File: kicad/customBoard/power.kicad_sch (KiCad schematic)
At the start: 30 parts

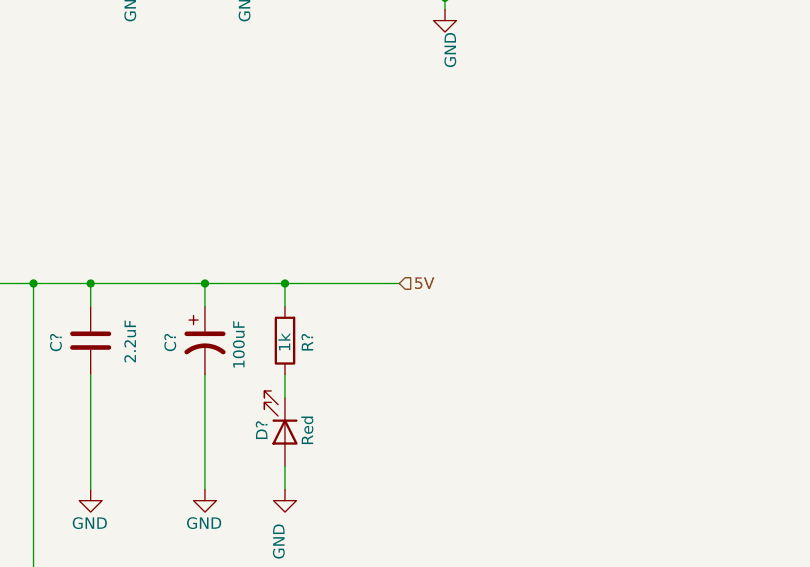
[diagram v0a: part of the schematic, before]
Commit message: First draft of CM4_GPIO
The CM4 connectors are split into two units. This is the right unit, name GPIO. Next is the left, High Speed Serial unit.
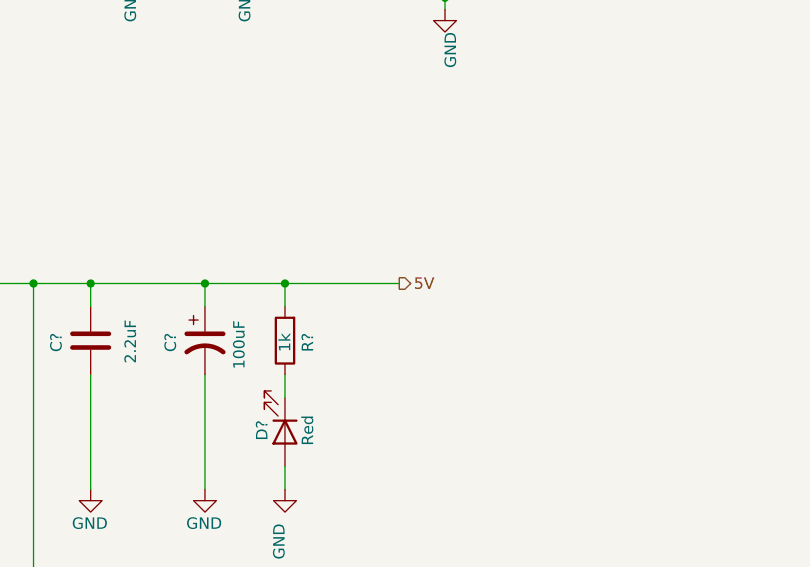
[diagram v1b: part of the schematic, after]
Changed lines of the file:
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@@
     (stroke (width 0) (type solid) (color 0 0 0 0))
   )
-  (hierarchical_label "5V" (shape input) (at 177.8 101.6 0)
+  (hierarchical_label "5V" (shape output) (at 177.8 101.6 0)
     (effects (font (size 1.27 1.27)) (justify left))
   )

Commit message: Generate Netlist
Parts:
- B1: renamed from B?; footprint (none) -> JSTPH2:JSTPH2
- C1, C2, C3, C4, C5, C6: renamed from C?; footprint (none) -> Capacitor_SMD:C_1206_3216Metric_Pad1.33x1.80mm_HandSolder
- D1, D2, D3, D4: renamed from D?; footprint (none) -> digikey-footprints:LED_5mm_Radial
- J1: renamed from J?; footprint GCT_USB4125-GF-A_REVA2 -> USB4125-GF-A_REVA2:GCT_USB4125-GF-A_REVA2
- L1: renamed from L?; footprint (none) -> NRS5030T6R8MMGJ:NRS5030T6R8MMGJ
- Q1: renamed from Q?; footprint SOT95P240X111-3N -> MMUN2133LT1G:SOT95P240X111-3N
- R1, R10, R11, R12, R13, R14, R2, R3, R4, R5, R6, R7, R8, R9: renamed from R?; footprint (none) -> Resistor_SMD:R_1206_3216Metric_Pad1.30x1.75mm_HandSolder
- U1: renamed from U?; footprint QFN65P400X400X100-17N -> TPS61090RSAR:QFN65P400X400X100-17N
- gave numbers to parts that had none: 1
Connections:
- no-connect marks 0 -> 1

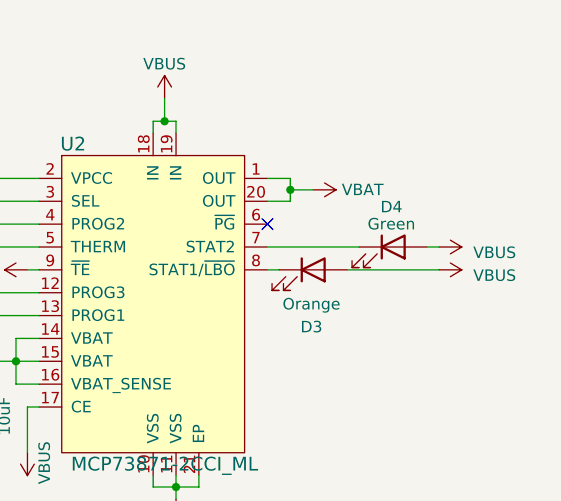
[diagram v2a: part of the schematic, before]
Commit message: Rework Power PCB and draft SD
Moving things around so they would make sense on the final board. Flipped around some of the power circuit so the battery can be plugged in on the left side to make room for all the ports on the right.
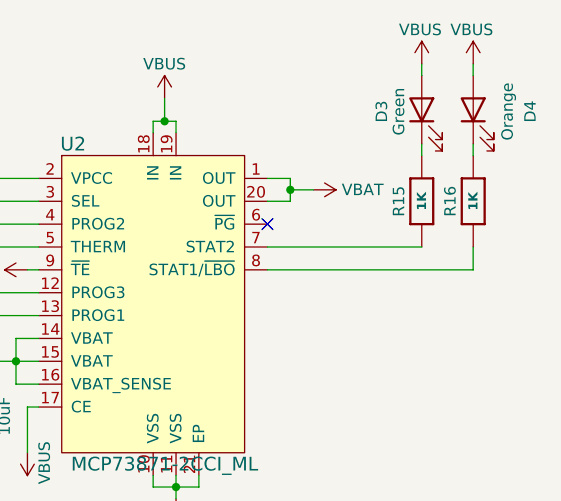
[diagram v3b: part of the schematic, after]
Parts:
- added R15, R16: 1K, Resistor_SMD:R_1206_3216Metric_Pad1.30x1.75mm_HandSolder, symbol Adafruit PowerBoost 1000C Rev B-eagle-import:RESISTOR0805_NOOUTLINE
- renumbered D4 to D3, D3 to D4
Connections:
- net at D4.1 (K): now also R16.1; no longer U2.8 (STAT1/~LBO)
- net at D3.1 (K): now also R15.1; no longer U2.7 (STAT2)
- new net: R16.2, U2.8 (STAT1/~LBO)
- new net: R15.2, U2.7 (STAT2)
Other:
- moved on the sheet: D3, D4
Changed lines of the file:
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@@
     (stroke (width 0) (type solid) (color 0 0 0 0))
   )
-  (wire (pts (xy 193.04 43.18) (xy 203.2 43.18))
-    (stroke (width 0) (type solid) (color 0 0 0 0))
-  )
-  (wire (pts (xy 193.04 45.72) (xy 194.31 45.72))
+  (wire (pts (xy 193.04 43.18) (xy 210.185 43.18))
+    (stroke (width 0) (type solid) (color 0 0 0 0))
+  )
+  (wire (pts (xy 193.04 45.72) (xy 215.9 45.72))
     (stroke (width 0) (type solid) (color 0 0 0 0))
   )
@@
     (stroke (width 0) (type solid) (color 0 0 0 0))
   )
-  (wire (pts (xy 201.93 45.72) (xy 212.09 45.72))
-    (stroke (width 0) (type solid) (color 0 0 0 0))
-  )
-  (wire (pts (xy 210.82 43.18) (xy 212.09 43.18))
+  (wire (pts (xy 210.185 22.86) (xy 210.185 24.13))
+    (stroke (width 0) (type solid) (color 0 0 0 0))
+  )
+  (wire (pts (xy 210.185 33.02) (xy 210.185 31.75))
+    (stroke (width 0) (type solid) (color 0 0 0 0))
+  )
+  (wire (pts (xy 215.9 24.13) (xy 215.9 22.86))
+    (stroke (width 0) (type solid) (color 0 0 0 0))
+  )
+  (wire (pts (xy 215.9 31.75) (xy 215.9 33.02))
+    (stroke (width 0) (type solid) (color 0 0 0 0))
+  )
+  (wire (pts (xy 215.9 43.18) (xy 215.9 45.72))
     (stroke (width 0) (type solid) (color 0 0 0 0))
   )
@@
     (pin "1")
   )
-  (symbol (lib_id "power:VBUS") (at 212.09 43.18 270) (unit 1)
-    (in_bom yes) (on_board yes) (fields_autoplaced)
-    (property "Reference" "#PWR032" (id 0) (at 208.28 43.18 0)
-      (effects (font (size 1.27 1.27)) hide)
-    )
-    (property "Value" "VBUS" (id 1) (at 215.9 43.8149 90)
-      (effects (font (size 1.27 1.27)) (justify left))
-    )
-    (property "Footprint" "" (id 2) (at 212.09 43.18 0)
-      (effects (font (size 1.27 1.27)) hide)
-    )
-    (property "Datasheet" "" (id 3) (at 212.09 43.18 0)
-      (effects (font (size 1.27 1.27)) hide)
-    )
-    (pin "1")
-  )
-  (symbol (lib_id "power:VBUS") (at 212.09 45.72 270) (unit 1)
-    (in_bom yes) (on_board yes) (fields_autoplaced)
-    (property "Reference" "#PWR033" (id 0) (at 208.28 45.72 0)
-      (effects (font (size 1.27 1.27)) hide)
-    )
-    (property "Value" "VBUS" (id 1) (at 215.9 46.3549 90)
-      (effects (font (size 1.27 1.27)) (justify left))
-    )
-    (property "Footprint" "" (id 2) (at 212.09 45.72 0)
-      (effects (font (size 1.27 1.27)) hide)
-    )
-    (property "Datasheet" "" (id 3) (at 212.09 45.72 0)
+  (symbol (lib_id "power:VBUS") (at 210.185 22.86 0) (unit 1)
+    (in_bom yes) (on_board yes)
+    (property "Reference" "#PWR032" (id 0) (at 210.185 26.67 0)
+      (effects (font (size 1.27 1.27)) hide)
+    )
+    (property "Value" "VBUS" (id 1) (at 207.6449 19.05 0)
+      (effects (font (size 1.27 1.27)) (justify left))
+    )
+    (property "Footprint" "" (id 2) (at 210.185 22.86 0)
+      (effects (font (size 1.27 1.27)) hide)
+    )
+    (property "Datasheet" "" (id 3) (at 210.185 22.86 0)
+      (effects (font (size 1.27 1.27)) hide)
+    )
+    (pin "1")
+  )
+  (symbol (lib_id "power:VBUS") (at 215.9 22.86 0) (unit 1)
+    (in_bom yes) (on_board yes)
+    (property "Reference" "#PWR033" (id 0) (at 215.9 26.67 0)
+      (effects (font (size 1.27 1.27)) hide)
+    )
+    (property "Value" "VBUS" (id 1) (at 213.3599 19.05 0)
+      (effects (font (size 1.27 1.27)) (justify left))
+    )
+    (property "Footprint" "" (id 2) (at 215.9 22.86 0)
+      (effects (font (size 1.27 1.27)) hide)
+    )
+    (property "Datasheet" "" (id 3) (at 215.9 22.86 0)
       (effects (font (size 1.27 1.27)) hide)
     )
@@
     (pin "2")
   )
+  (symbol (lib_id "Adafruit PowerBoost 1000C Rev B-eagle-import:RESISTOR0805_NOOUTLINE") (at 210.185 38.1 270) (unit 1)
+    (in_bom yes) (on_board yes)
+    (property "Reference" "R15" (id 0) (at 207.645 38.1 0))
+    (property "Value" "1K" (id 1) (at 210.185 38.1 0)
+      (effects (font (size 1.016 1.016) bold))
+    )
+    (property "Footprint" "Resistor_SMD:R_1206_3216Metric_Pad1.30x1.75mm_HandSolder" (id 2) (at 210.185 38.1 0)
+      (effects (font (size 1.27 1.27)) hide)
+    )
+    (property "Datasheet" "" (id 3) (at 210.185 38.1 0)
+      (effects (font (size 1.27 1.27)) hide)
+    )
+    (pin "1")
+    (pin "2")
+  )
+  (symbol (lib_id "Adafruit PowerBoost 1000C Rev B-eagle-import:RESISTOR0805_NOOUTLINE") (at 215.9 38.1 270) (unit 1)
+    (in_bom yes) (on_board yes)
+    (property "Reference" "R16" (id 0) (at 213.36 38.1 0))
+    (property "Value" "1K" (id 1) (at 215.9 38.1 0)
+      (effects (font (size 1.016 1.016) bold))
+    )
+    (property "Footprint" "Resistor_SMD:R_1206_3216Metric_Pad1.30x1.75mm_HandSolder" (id 2) (at 215.9 38.1 0)
+      (effects (font (size 1.27 1.27)) hide)
+    )
+    (property "Datasheet" "" (id 3) (at 215.9 38.1 0)
+      (effects (font (size 1.27 1.27)) hide)
+    )
+    (pin "1")
+    (pin "2")
+  )
   (symbol (lib_id "JSTPH2:BATTERY") (at 147.32 62.23 90) (unit 1)
     (in_bom yes) (on_board yes)
@@
     (pin "2")
   )
-  (symbol (lib_id "Device:LED") (at 198.12 45.72 0) (unit 1)
-    (in_bom yes) (on_board yes)
-    (property "Reference" "D3" (id 0) (at 197.9295 52.07 0))
-    (property "Value" "Orange" (id 1) (at 197.9295 49.53 0))
-    (property "Footprint" "digikey-footprints:LED_5mm_Radial" (id 2) (at 198.12 45.72 0)
-      (effects (font (size 1.27 1.27)) hide)
-    )
-    (property "Datasheet" "~" (id 3) (at 198.12 45.72 0)
-      (effects (font (size 1.27 1.27)) hide)
-    )
-    (pin "1")
-    (pin "2")
-  )
-  (symbol (lib_id "Device:LED") (at 207.01 43.18 0) (unit 1)
-    (in_bom yes) (on_board yes)
-    (property "Reference" "D4" (id 0) (at 206.8195 38.735 0))
-    (property "Value" "Green" (id 1) (at 206.8195 40.64 0))
-    (property "Footprint" "digikey-footprints:LED_5mm_Radial" (id 2) (at 207.01 43.18 0)
-      (effects (font (size 1.27 1.27)) hide)
-    )
-    (property "Datasheet" "~" (id 3) (at 207.01 43.18 0)
-      (effects (font (size 1.27 1.27)) hide)
-    )
+  (symbol (lib_id "Device:LED") (at 210.185 27.94 90) (unit 1)
+    (in_bom yes) (on_board yes)
+    (property "Reference" "D3" (id 0) (at 205.74 28.1305 0))
+    (property "Value" "Green" (id 1) (at 207.645 28.1305 0))
+    (property "Footprint" "digikey-footprints:LED_5mm_Radial" (id 2) (at 210.185 27.94 0)
+      (effects (font (size 1.27 1.27)) hide)
+    )
+    (property "Datasheet" "~" (id 3) (at 210.185 27.94 0)
+      (effects (font (size 1.27 1.27)) hide)
+    )
+    (pin "1")
+    (pin "2")
+  )
+  (symbol (lib_id "Device:LED") (at 215.9 27.94 90) (unit 1)
+    (in_bom yes) (on_board yes)
+    (property "Reference" "D4" (id 0) (at 222.25 28.1305 0))
+    (property "Value" "Orange" (id 1) (at 219.71 28.1305 0))
+    (property "Footprint" "digikey-footprints:LED_5mm_Radial" (id 2) (at 215.9 27.94 0)
+      (effects (font (size 1.27 1.27)) hide)
+    )
+    (property "Datasheet" "~" (id 3) (at 215.9 27.94 0)
+      (effects (font (size 1.27 1.27)) hide)
+    )

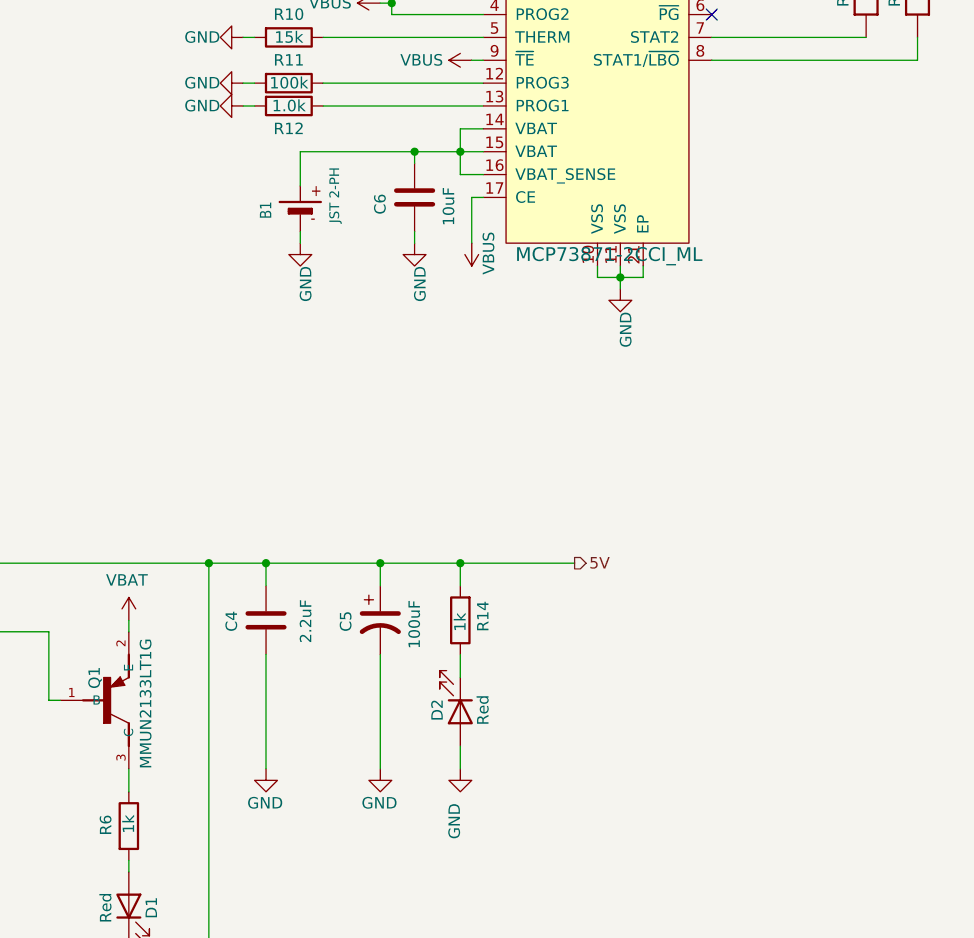
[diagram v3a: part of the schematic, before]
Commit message: Updates based on meeting with Dr. Jordan
Everything should be good to go now, next up is generating a bill of materials (making sure everything is in stock), and generating gerbers
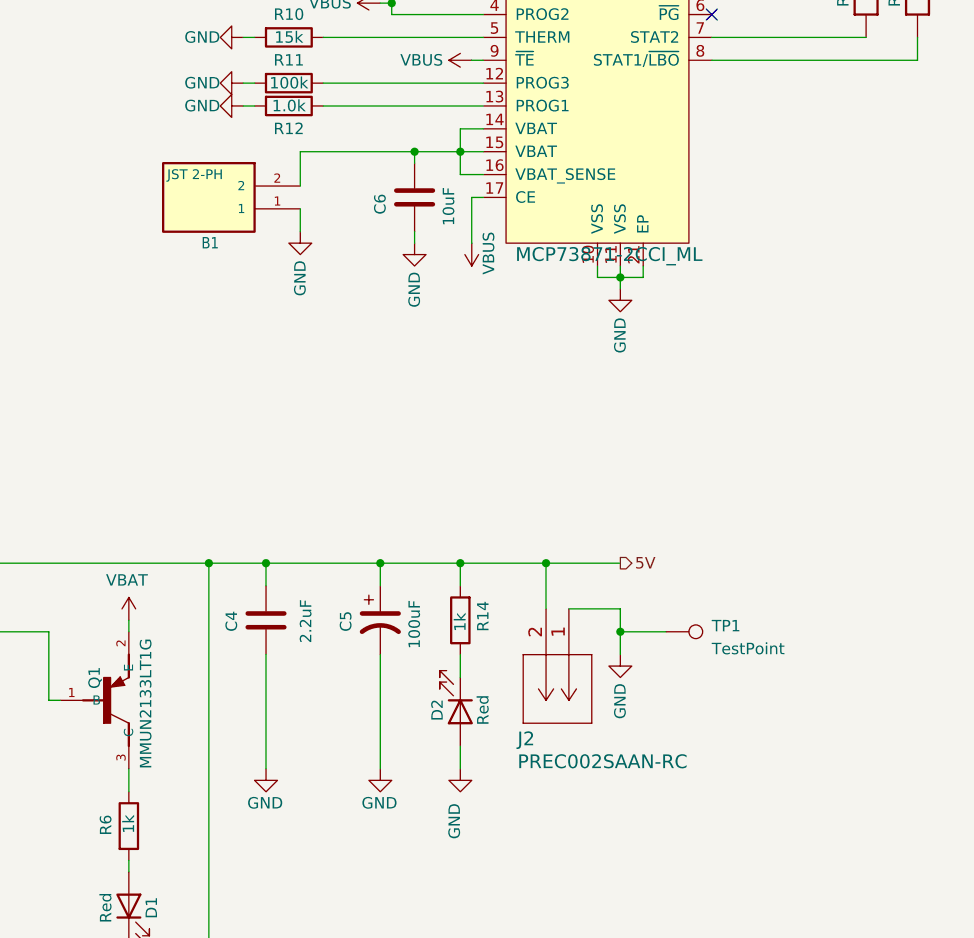
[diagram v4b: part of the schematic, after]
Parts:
- added J2: PREC002SAAN-RC, PREC002SAAN-RC:PREC002SAAN-RC, symbol PREC002SAAN-RC:PREC002SAAN-RC
- added TP1: TestPoint, TestPoint:TestPoint_Pad_4.0x4.0mm, symbol Connector:TestPoint
- B1: footprint JSTPH2:JSTPH2 -> JST_S2B-PH-K-S(LF)(SN):JST_S2B-PH-K-S(LF)(SN); symbol JSTPH2:BATTERY -> S2B-PH-K-S_LF__SN_:S2B-PH-K-S(LF)(SN); AVAILABILITY (none) -> Unavailable; DESCRIPTION (none) -> Connector Header Through Hole, Right Angle 2 position; MAXIMUM_PACKAGE_HEIGHT (none) -> 4.8mm; MF (none) -> JST Sales; MP (none) -> S2B-PH-K-S_LF__SN_; PACKAGE (none) -> None; PRICE (none) -> None
- D1, D2, D3, D4: footprint digikey-footprints:LED_5mm_Radial -> LED_SMD:LED_1206_3216Metric_Pad1.42x1.75mm_HandSolder
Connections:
- net 5V: now also J2.2
- net GND: now also J2.1, TP1.1

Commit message: Generate BOM
Clean up all the part data and add manufacturer's numbers for ordering
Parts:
- B1: AVAILABILITY Unavailable -> (none); DESCRIPTION Connector Header Through Hole, Right Angle 2 position -> (none); MAXIMUM_PACKAGE_HEIGHT 4.8mm -> (none); MF JST Sales -> (none); MP S2B-PH-K-S_LF__SN_ -> (none); PACKAGE None -> (none); PRICE None -> (none); manf# (none) -> B2B-PH-K-S(LF)(SN)
- C1, C3, C6: manf# (none) -> CL31B106MOHNNNE
- C2: manf# (none) -> CL31B104KBCNFNC
- C4: manf# (none) -> CL31B225KOHNNNE
- C5: manf# (none) -> GRM31CR60G107ME39L
- D1, D2: manf# (none) -> 156120RS75300
- D3: manf# (none) -> 150120GS75000
- D4: manf# (none) -> 150120AS75000
- J1: MANUFACTURER GCT -> (none); MAXIMUM_PACKAGE_HEIGHT 3.16 mm -> (none); PARTREV Rev A2 -> (none); STANDARD Manufacturer Recommendations -> (none); manf# (none) -> USB4125-GF-A
- J2: manf# (none) -> PREC002SAAN-RC
- L1: manf# (none) -> NRS5030T6R8MMGJ
- Q1: MANUFACTURER ON Semiconductor -> (none); manf# (none) -> MMUN2133LT1G
- R1, R7: manf# (none) -> RC1206FR-071M87L
- R10: value 15k -> 15K; manf# (none) -> RC1206FR-0715KL
- R11, R9: value 100k -> 100K; manf# (none) -> RMCF1206FT100K
- R12: value 1.0k -> 1K; manf# (none) -> RC1206FR-071KL
- R13: value 270k -> 270K; manf# (none) -> RC1206FR-07270KL
- R14, R6: value 1k -> 1K; manf# (none) -> RC1206FR-071KL
- R15, R16: manf# (none) -> RC1206FR-071KL
- R2: value 340k -> 340K; manf# (none) -> ERJ-8ENF3403V
- R3, R4: value 5.1k -> 5.1K; manf# (none) -> RMCF1206FT5K10
- R5, R8: value 200k -> 200K; manf# (none) -> RC1206FR-07200KL
- U1: AVAILABILITY Good -> (none); DESCRIPTION 2A Switch, 96% Efficient Boost Converter 16-QFN -40 to 85 -> (none); MF Texas Instruments -> (none); MP TPS61090RSAR -> (none); PACKAGE VQFN-16 Texas Instruments -> (none); PRICE 1.48 USD -> (none); SNAPEDA_PACKAGE_ID 22461 -> (none); manf# (none) -> TPS61090RSAR
- U2: Category Integrated Circuits (ICs) -> (none); DK_Datasheet_Link http://www.microchip.com/mymicrochip/filehandler.aspx?ddocn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 -> (none); DK_Detail_Page /product-detail/en/microchip-technology/MCP73871-2CCI-ML/MC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 -> (none); Digi-Key_PN MCP73871-2CCI/ML-ND -> (none); Family PMIC - Battery Chargers -> (none); MPN MCP73871-2CCI/ML -> (none); Manufacturer Microchip Technology -> (none); Status Active -> (none); manf# (none) -> MCP73871-2CCI/ML
